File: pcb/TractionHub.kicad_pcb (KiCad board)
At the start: 2 copper layers, 90 parts, among them IC1 DRV8302DCA, J1 Conn_01x05, J2 Conn_ARM_SWD_TagConnect_TC2030, J3 MAIN_PWR_CON, J4 Conn_01x03, J5 USB_C_Receptacle_USB2.0_14P, J6 Conn_01x06, Q1 IRFR7540TRPBF, Q2 IRFR7540TRPBF, Q3 IRFR7540TRPBF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

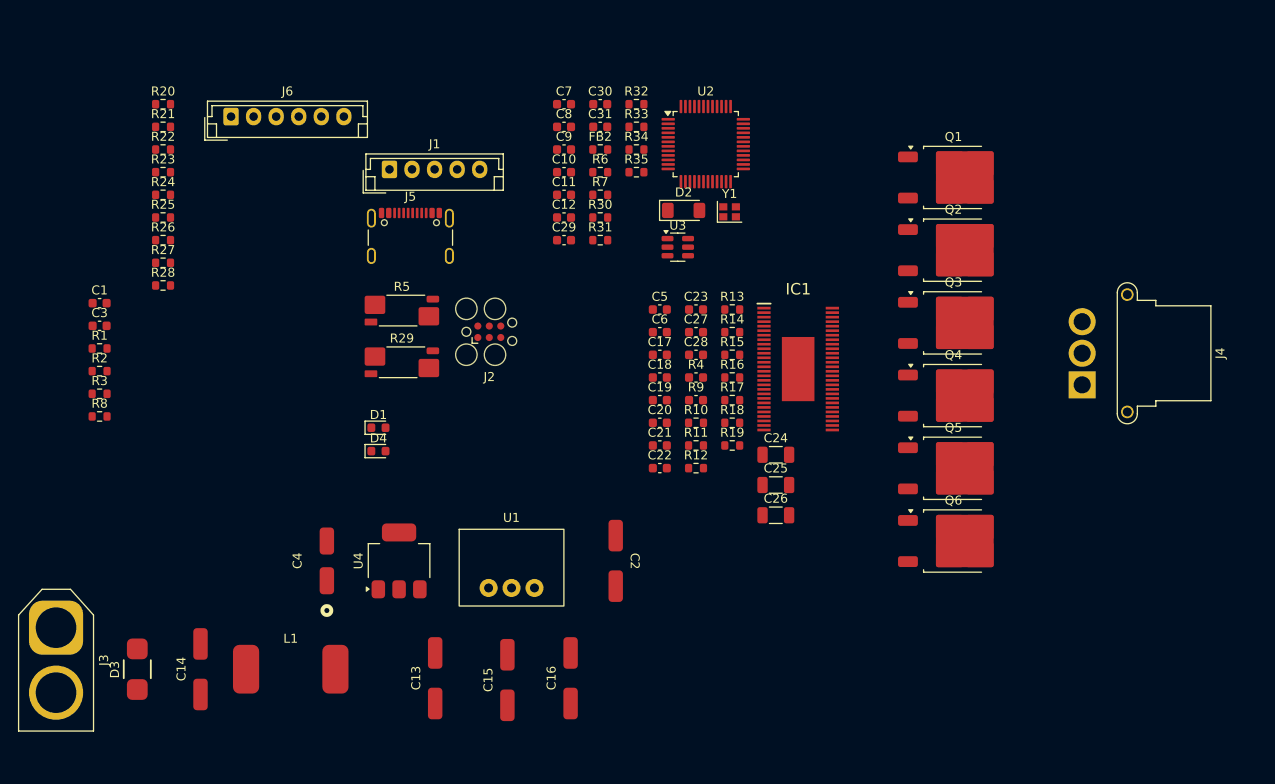
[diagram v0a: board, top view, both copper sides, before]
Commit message: pcb: outlines ready
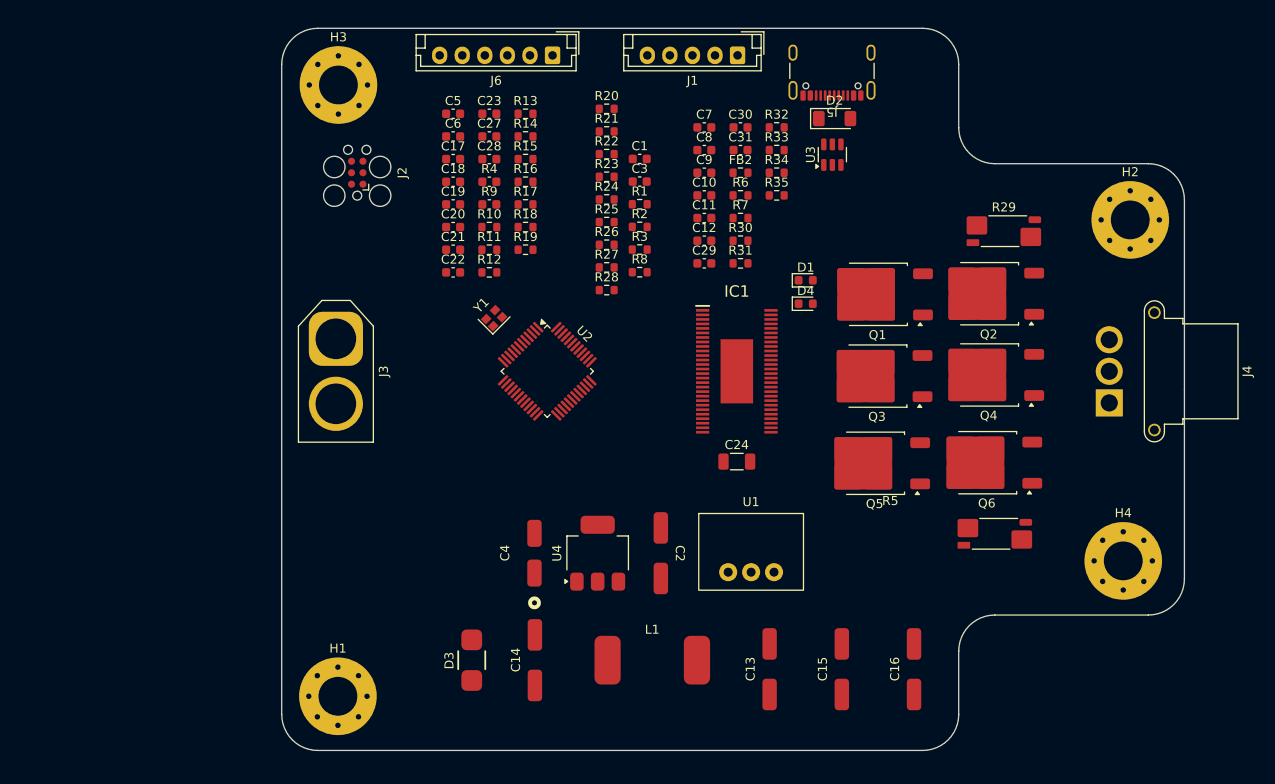
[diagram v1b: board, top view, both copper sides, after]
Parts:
- removed C25, C26: 10u/50V, Capacitor_SMD:C_1206_3216Metric
- added H1: MountingHole_Pad, MountingHole:MountingHole_4.3mm_M4_Pad_Via, F.Cu at (133.2, 131.0)
- added H2: MountingHole_Pad, MountingHole:MountingHole_4.3mm_M4_Pad_Via, F.Cu at (221.0, 78.2)
- added H3: MountingHole_Pad, MountingHole:MountingHole_4.3mm_M4_Pad_Via, F.Cu at (133.3, 63.3)
- added H4: MountingHole_Pad, MountingHole:MountingHole_4.3mm_M4_Pad_Via, F.Cu at (220.2, 116.0)
- C1: value 10n -> 100nF
- moved R5 70.2 mm to (206.0, 113.0)
- moved R29 68.2 mm to (207.0, 79.5)
- moved C1 61.9 mm to (166.7, 71.5)
- moved R1 61.9 mm to (166.7, 76.5)
- moved R2 61.9 mm to (166.7, 79.0)
- moved R8 61.9 mm to (166.7, 84.0)
- moved C3 61.9 mm to (166.7, 74.0)
- moved R3 61.9 mm to (166.7, 81.5)
- moved J5 50.9 mm to (188.0, 60.8), turned to 180 degrees
- moved D1 50.1 mm to (185.0, 84.9)
- moved D4 50.1 mm to (185.0, 87.5)
- moved R20 49.1 mm to (163.0, 65.9)
- moved R21 49.1 mm to (163.0, 68.4)
- moved R22 49.1 mm to (163.0, 70.9)
- moved R23 49.1 mm to (163.0, 73.5)
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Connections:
- J4 pad 1: /bridge/H1_VS -> /bridge/H3_VS
- J4 pad 3: /bridge/H3_VS -> /bridge/H1_VS
- Q1 pad 1: VCC -> Net-(Q1-G)
- Q1 pad 2: Net-(Q1-G) -> VCC
- Q2 pad 1: /bridge/H1_VS -> Net-(Q2-G)
- Q2 pad 2: Net-(Q2-G) -> /bridge/H1_VS
- Q3 pad 1: VCC -> Net-(Q3-G)
- Q3 pad 2: Net-(Q3-G) -> VCC
- Q4 pad 1: /bridge/H2_VS -> Net-(Q4-G)
- Q4 pad 2: Net-(Q4-G) -> /bridge/H2_VS
- Q5 pad 1: VCC -> Net-(Q5-G)
- Q5 pad 2: Net-(Q5-G) -> VCC
- Q6 pad 1: /bridge/H3_VS -> Net-(Q6-G)
- Q6 pad 2: Net-(Q6-G) -> /bridge/H3_VS
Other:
- board outline added: 100 x 80 mm

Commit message: pcb: layout wip
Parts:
- moved D2 57.7 mm to (132.2, 81.0)
- moved R22 53.2 mm to (197.5, 111.5)
- moved U3 51.3 mm to (138.0, 82.5)
- moved R21 47.8 mm to (197.5, 101.5)
- moved R20 42.9 mm to (197.5, 91.5)
- moved D4 38.5 mm to (172.8, 124.0)
- moved J5 38.0 mm to (150.0, 59.5)
- moved D1 36.9 mm to (159.5, 111.5)
- moved J6 19.0 mm to (176.0, 60.0)
- moved J1 16.5 mm to (194.0, 60.0)
- moved J3 9.25 mm to (134.0, 100.6), turned to 90 degrees
- moved D3 4.65 mm to (144.5, 130.0)
- moved C4 4.41 mm to (151.0, 117.0), turned to -90 degrees
- moved C14 3.94 mm to (152.5, 130.0)
- moved L1 3.63 mm to (166.0, 130.0)
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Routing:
- added copper zone on F.Cu, net /bridge/H1_VS
- added copper zone on F.Cu, net /bridge/H2_VS
- added copper zone on F.Cu, net /bridge/H3_VS
- added copper zone on F.Cu, net /power/+VDC
- added copper zone on F.Cu, net VCC

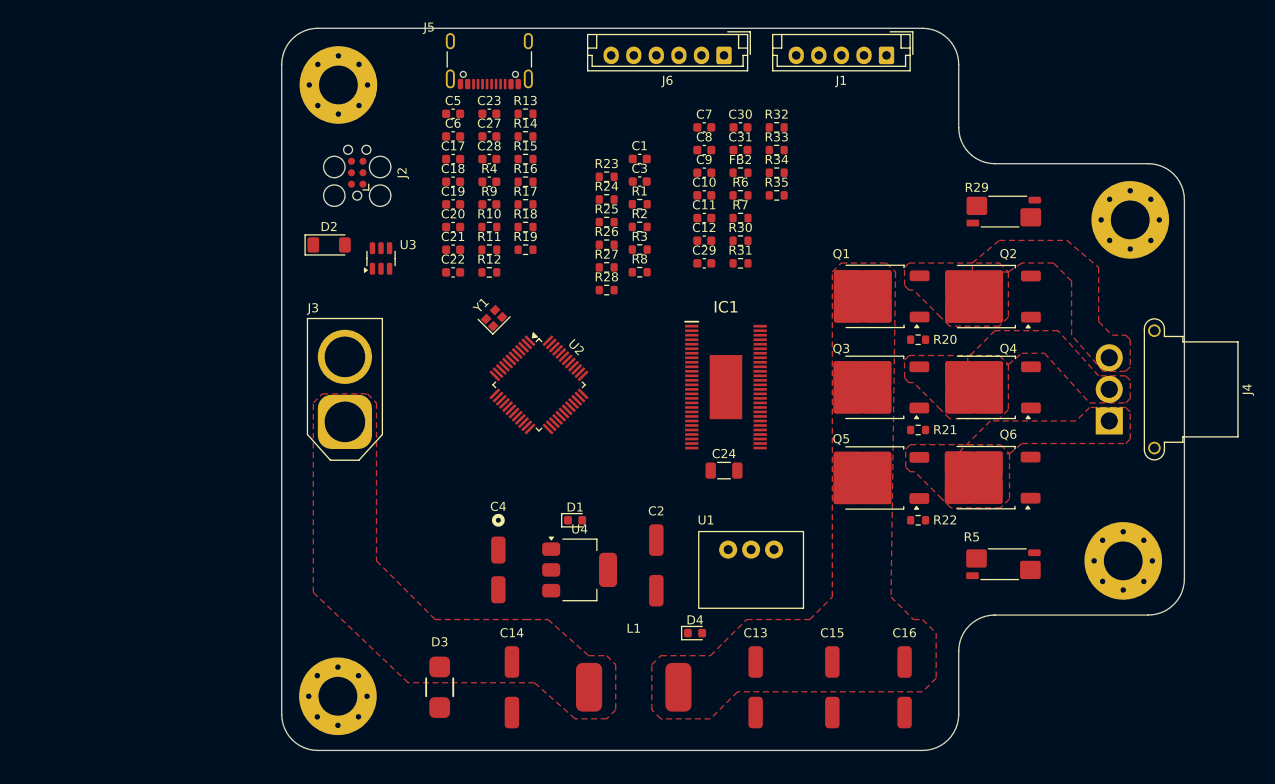
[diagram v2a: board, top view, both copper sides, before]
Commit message: pcb: layout power
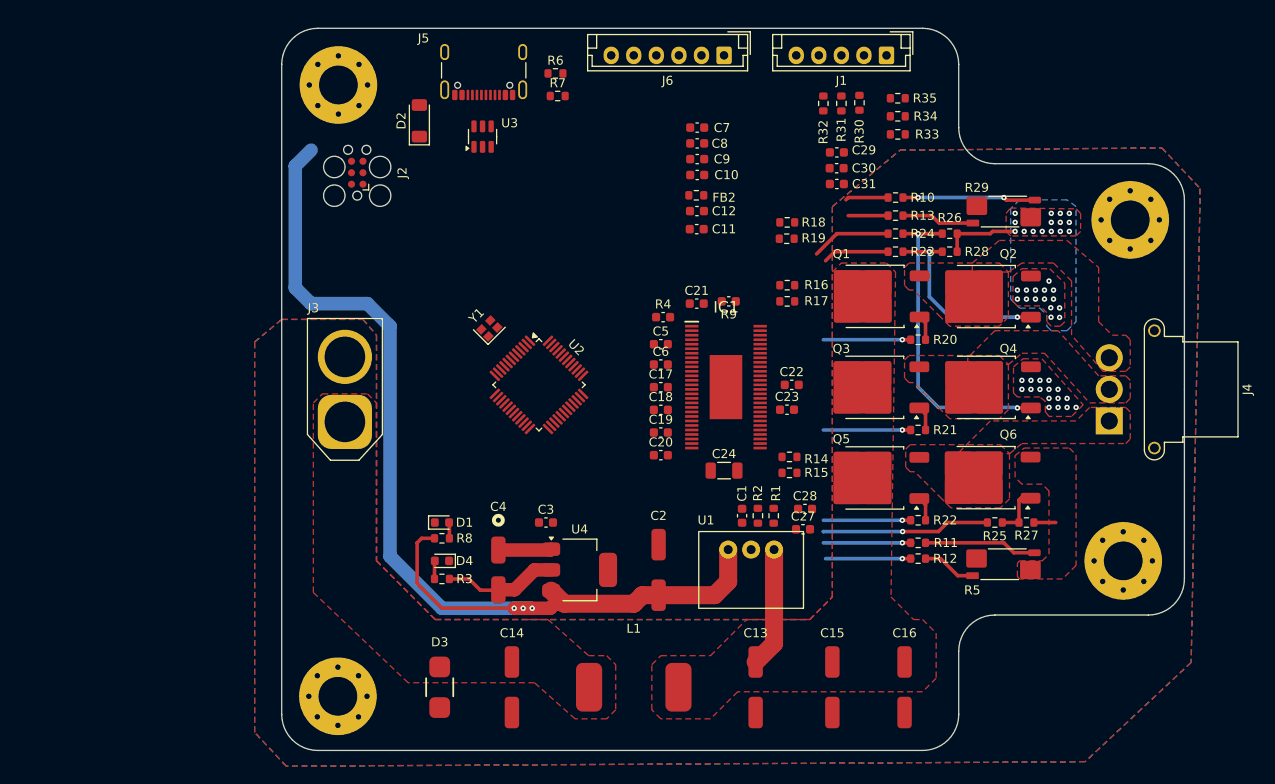
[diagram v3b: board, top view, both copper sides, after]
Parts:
- moved R11 57.5 mm to (197.5, 114.0)
- moved R12 57.1 mm to (197.5, 115.8)
- moved C27 55.7 mm to (184.8, 112.5)
- moved R27 54.4 mm to (209.5, 111.8), turned to 180 degrees
- moved R25 54.4 mm to (206.0, 111.8)
- moved C28 52.2 mm to (185.0, 110.2)
- moved C23 46.5 mm to (183.0, 99.2)
- moved R14 46.0 mm to (183.2, 104.5)
- moved R15 45.4 mm to (183.2, 106.2)
- moved R10 45.1 mm to (195.0, 75.8)
- moved R3 42.6 mm to (144.8, 118.0), turned to 180 degrees
- moved R13 42.5 mm to (195.0, 77.8)
- moved C1 41.1 mm to (178.0, 111.0), turned to -90 degrees
- moved C22 39.5 mm to (183.5, 96.5)
- moved C3 39.2 mm to (156.3, 111.8)
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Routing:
- net +5V: track 0.00 -> 120.9 mm, vias 0 -> 3
- net Net-(Q4-G): track 0.00 -> 34.8 mm, vias 0 -> 2
- net Net-(Q2-G): track 0.00 -> 21.5 mm, vias 0 -> 2
- net /bridge/M_L3: track 0.00 -> 18.6 mm, vias 0 -> 1
- net /mosfet_driver/SH1_A: track 0.00 -> 14.7 mm, vias 0 -> 2
- net VCC: track 0.00 -> 13.3 mm
- net VDD: track 0.00 -> 12.7 mm
- net /mosfet_driver/SH1_B: track 0.00 -> 12.3 mm
- net Net-(IC1-SP1): track 0.00 -> 9.93 mm, vias 0 -> 1
- net Net-(IC1-SN2): track 0.00 -> 9.68 mm, vias 0 -> 1
- net /bridge/M_H3: track 0.00 -> 9.68 mm, vias 0 -> 1
- net /bridge/M_H2: track 0.00 -> 9.68 mm, vias 0 -> 1
- net /bridge/M_H1: track 0.00 -> 9.68 mm, vias 0 -> 1
- net /bridge/M_L2: track 0.00 -> 8.86 mm
- net /bridge/H1_LOW: track 0.00 -> 8.53 mm, vias 0 -> 30
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- added copper zone on B.Cu, net /bridge/H1_LOW
- added copper zone on F.Cu, net /bridge/H1_LOW
- added copper zone on F.Cu, net /bridge/H3_LOW
- added copper zone on B.Cu, net GND
- added copper zone on F.Cu, net GND

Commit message: pcb: layout gate driver
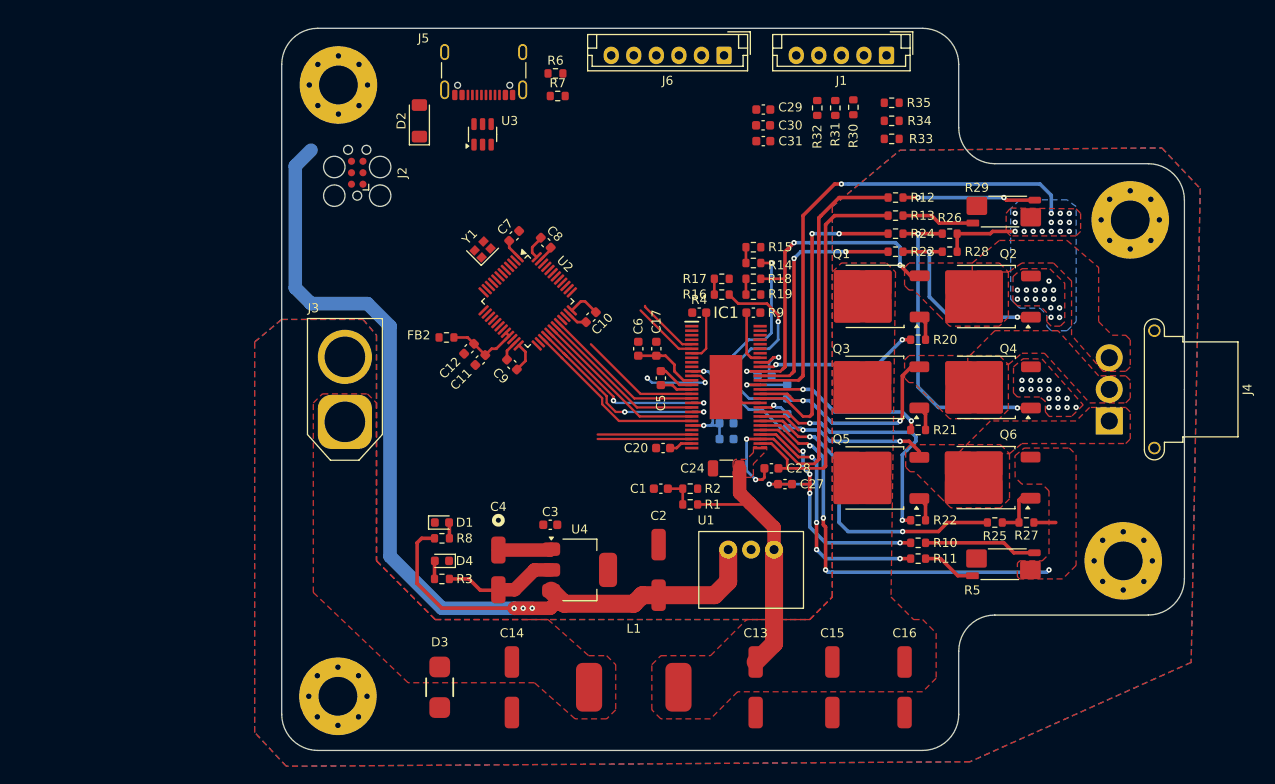
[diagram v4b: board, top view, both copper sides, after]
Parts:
- C18, C19, C21, C22, C23: moved to B.Cu
- U4: value TC2117-3.3VDBTR -> TC2117-3.3VDBTR
- moved R12 40.1 mm to (195.0, 75.8)
- moved R10 38.3 mm to (197.5, 114.0)
- moved FB2 31.8 mm to (145.2, 91.2), turned to 180 degrees
- moved C9 30.6 mm to (152.5, 94.2), turned to 135 degrees
- moved C12 29.5 mm to (147.8, 92.5), turned to -135 degrees
- moved C11 28.0 mm to (149.0, 93.8), turned to -135 degrees
- moved R15 25.3 mm to (179.2, 81.2)
- moved C7 23.6 mm to (152.8, 80.0), turned to 45 degrees
- moved R14 21.8 mm to (179.2, 83.0)
- moved C8 20.1 mm to (156.2, 80.8), turned to -45 degrees
- moved C10 19.7 mm to (161.2, 89.0), turned to -135 degrees
- moved C21 11.0 mm to (180.5, 95.5), turned to 180 degrees
- moved C1 9.49 mm to (169.0, 108.0), turned to 180 degrees
- moved C29 9.43 mm to (180.3, 66.0)
- moved C30 9.43 mm to (180.3, 67.8)
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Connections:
- R29 pad 3: /mosfet_driver/SH1_A -> /mosfet_driver/SH2_A
- R5 pad 2: /mosfet_driver/SH2_A -> /mosfet_driver/SH1_B
- R5 pad 3: /mosfet_driver/SH1_B -> /mosfet_driver/SH1_A
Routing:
- net /bridge/H1_LOW: track 8.53 -> 62.7 mm, vias 30 -> 31
- net /bridge/H2_VS: track 0.00 -> 49.4 mm, vias 0 -> 3
- net /bridge/H3_VS: track 0.00 -> 47.8 mm, vias 0 -> 3
- net /bridge/H3_LOW: track 2.43 -> 48.4 mm, vias 0 -> 4
- net Net-(IC1-SN2): track 9.68 -> 51.7 mm, vias 1 -> 2
- net Net-(IC1-SP2): track 4.43 -> 44.1 mm
- net /bridge/H1_VS: track 0.00 -> 39.3 mm, vias 0 -> 3
- net /bridge/M_L2: track 8.86 -> 35.1 mm, vias 0 -> 2
- net Net-(IC1-SP1): track 9.93 -> 35.3 mm, vias 1 -> 5
- net /microcontroller/L2: track 0.00 -> 23.2 mm, vias 0 -> 2
- net Net-(IC1-SN1): track 4.78 -> 27.3 mm, vias 0 -> 4
- net /microcontroller/L1: track 0.00 -> 21.9 mm, vias 0 -> 2
- net /microcontroller/L3: track 0.00 -> 20.7 mm
- net /bridge/M_L1: track 7.34 -> 27.2 mm, vias 0 -> 2
- net /bridge/M_H3: track 9.68 -> 29.2 mm, vias 1 -> 2
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
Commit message: pcb: v1.0 layout finsihed
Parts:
- added REF**: ESD-Logo_6.6x6mm_SilkScreen, Symbol:ESD-Logo_6.6x6mm_SilkScreen, F.Cu at (221.8, 85.8)
- moved R34 17.8 mm to (177.2, 71.5), turned to -90 degrees
- moved R35 15.4 mm to (180.5, 71.5), turned to -90 degrees
- moved R7 14.6 mm to (143.2, 61.5), turned to -90 degrees
- moved R33 11.1 mm to (183.8, 71.5), turned to -90 degrees
- moved FB2 6.21 mm to (150.0, 95.2), turned to -135 degrees
- moved C31 4.50 mm to (180.5, 65.0), turned to 90 degrees
- moved C30 4.13 mm to (177.2, 65.0), turned to 90 degrees
- moved J2 4.00 mm to (135.2, 77.0), turned to -90 degrees
- moved D2 3.91 mm to (145.2, 69.8)
- moved C29 3.54 mm to (183.8, 65.0), turned to 90 degrees
- moved R30 2.11 mm to (191.5, 64.0)
- moved R31 1.95 mm to (189.0, 64.0)
- moved R32 1.83 mm to (186.5, 64.0)
- moved R6 1.42 mm to (156.0, 61.5), turned to -90 degrees
- moved U3 1.03 mm to (149.5, 69.8)
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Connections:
- U3 pad 1: /microcontroller/USBC_D- -> /microcontroller/USB_D+
- U3 pad 2: GND -> /microcontroller/VBUS
- U3 pad 3: /microcontroller/USBC_D+ -> /microcontroller/USB_D-
- U3 pad 4: /microcontroller/USB_D+ -> /microcontroller/USBC_D-
- U3 pad 5: +5V -> GND
- U3 pad 6: /microcontroller/USB_D- -> /microcontroller/USBC_D+
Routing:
- net GND: track 17.2 -> 143.8 mm, vias 16 -> 53
- net +5V: track 120.9 -> 198.6 mm, vias 3 -> 10
- net /microcontroller/SENS1: track 1.75 -> 53.2 mm, vias 0 -> 2
- net Net-(U2-PB6): track 0.00 -> 49.3 mm, vias 0 -> 4
- net /microcontroller/SENS2: track 1.75 -> 50.9 mm, vias 0 -> 2
- net /microcontroller/SENS3: track 1.75 -> 50.2 mm, vias 0 -> 4
- net Net-(U2-PB7): track 0.00 -> 47.2 mm, vias 0 -> 5
- net Net-(U2-PB5): track 0.00 -> 44.1 mm, vias 0 -> 4
- net /microcontroller/VCC_SENSE: track 3.40 -> 46.4 mm
- net /microcontroller/SWDIO: track 0.00 -> 42.9 mm
- net /microcontroller/UART_TX: track 0.00 -> 42.6 mm, vias 0 -> 4
- net /microcontroller/UART_RX: track 0.00 -> 40.7 mm, vias 0 -> 3
- net /microcontroller/USB_D-: track 0.00 -> 39.3 mm
- net /microcontroller/SWD_RST: track 0.00 -> 38.7 mm, vias 0 -> 2
- net /microcontroller/USB_D+: track 0.00 -> 38.2 mm
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- added copper zone on B.Cu, net VDD
- added copper zone on F.Cu, net VDD
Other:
- board text added: "David Mezler"
- board text added: "HALL"
- board text added: "STM32G4"
- board text added: "USB-C"
- board text added: "Ver 1.0"
- board text added: "XT60"
- board text added: "traction-hub"
